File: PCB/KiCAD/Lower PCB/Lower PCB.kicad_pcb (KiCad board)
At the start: 2 copper layers, 188.6 x 165.4 mm, 106 parts, among them IC1 ADG608BRZ, IC2 ADG608BRZ, IC3 ADG608BRZ, J1 Conn_01x02_MountingPin, J2 Conn_01x04_MountingPin, J3 Conn_01x04_MountingPin, J4 Conn_01x04_MountingPin, Q1 SFH320, Q10 SFH320, Q11 SFH320, Q12 SFH320, Q13 SFH320, Q14 SFH320, Q15 SFH320, Q16 SFH320, Q17 SFH320, Q18 SFH320, Q19 SFH320, Q2 SFH320, Q20 SFH320, Q21 SFH320, Q22 SFH320, Q23 SFH320, Q24 SFH320, Q3 SFH320, Q4 SFH320, Q5 SFH320, Q6 SFH320, Q7 SFH320, Q8 SFH320, Q9 SFH320

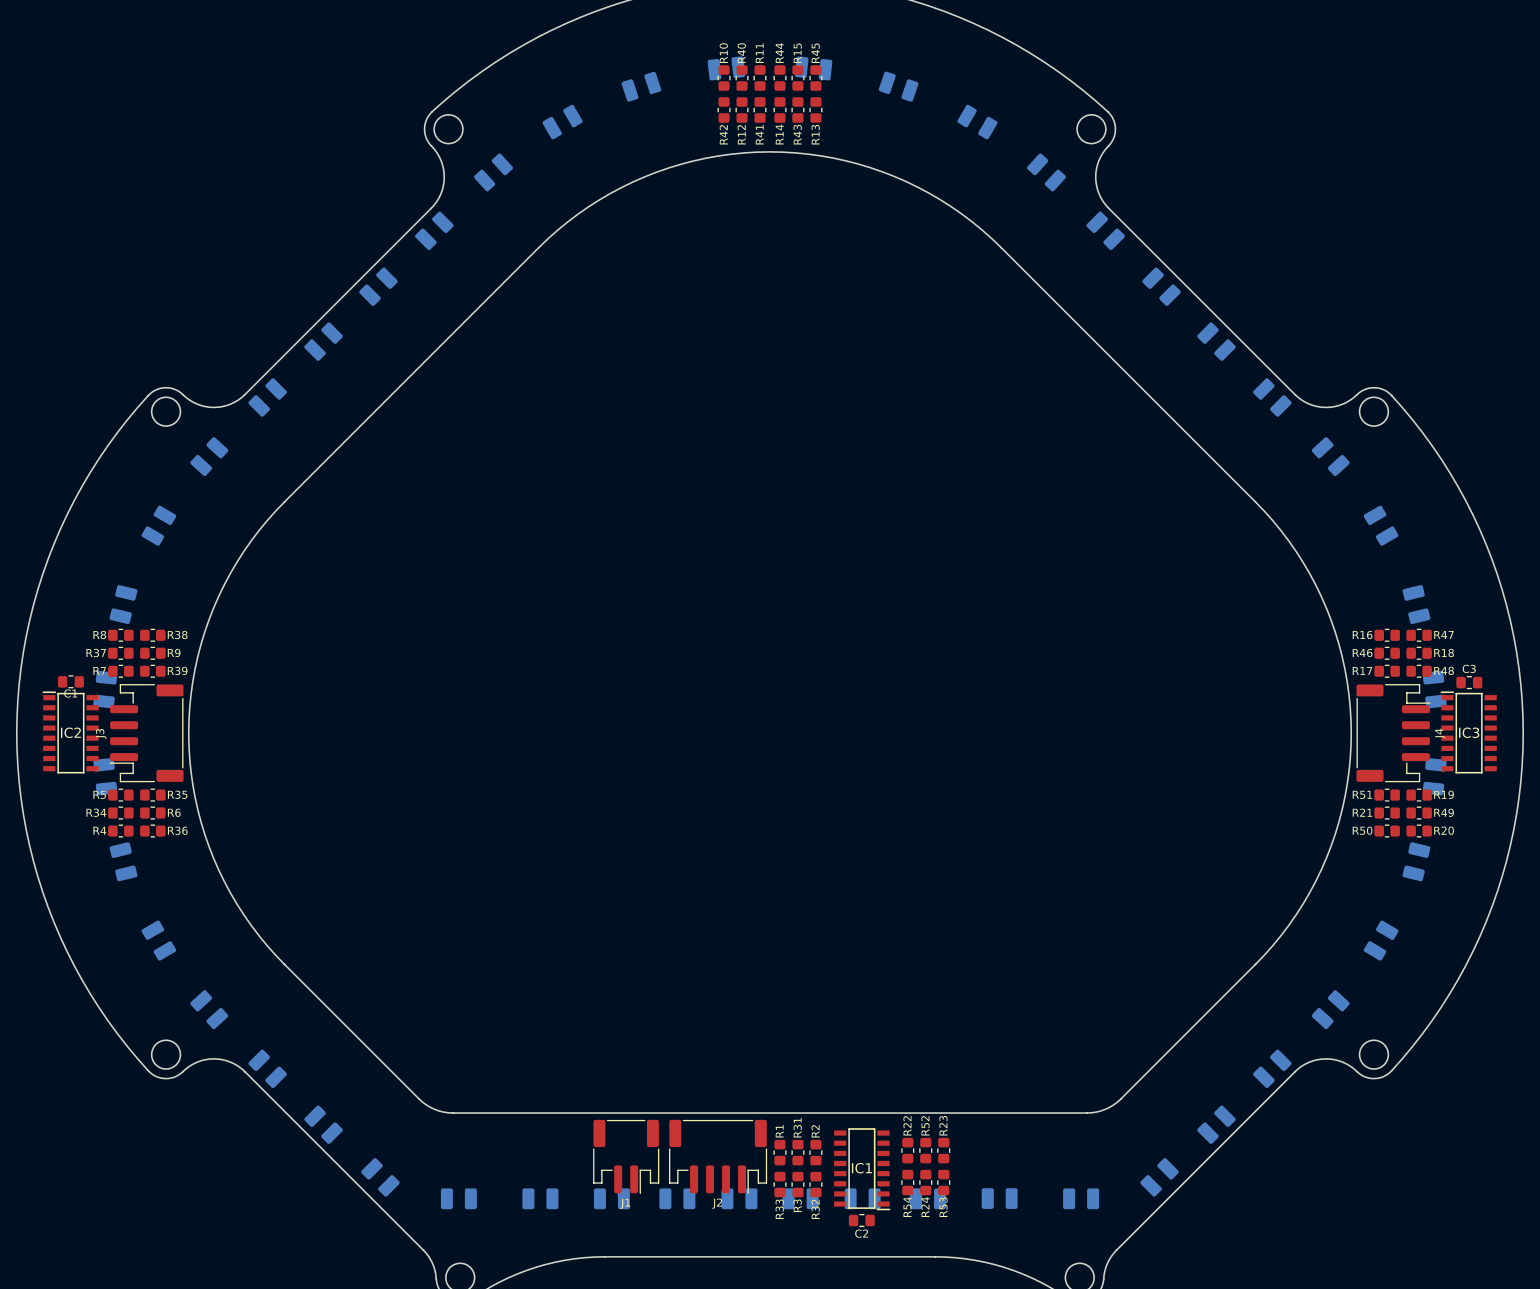
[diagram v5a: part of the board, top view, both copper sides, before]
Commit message: Started routing lower PCB
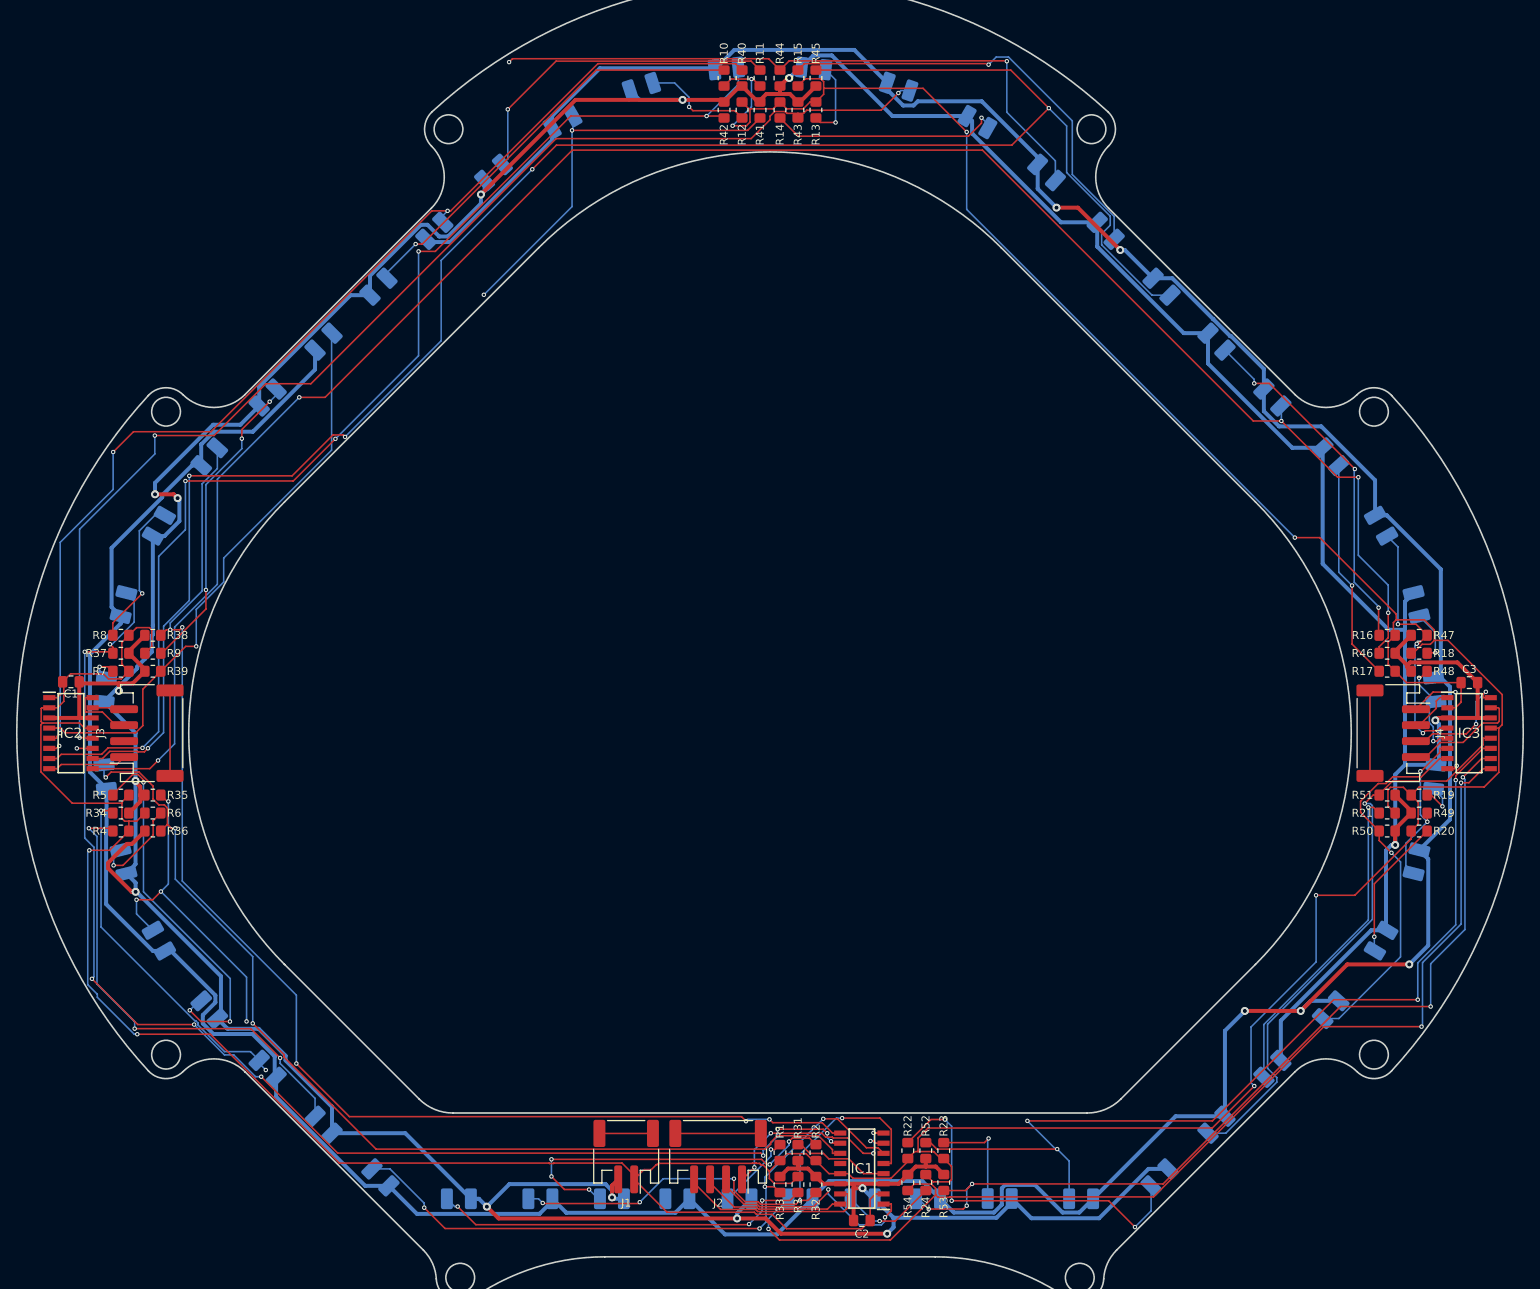
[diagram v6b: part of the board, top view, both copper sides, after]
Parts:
- turned D8 to 60 degrees
- turned Q5 to 120 degrees
- turned D20 to -121 degrees
- turned Q17 to -60 degrees
- turned D14 to -30 degrees
- turned Q11 to 30 degrees
- turned D11 to 42 degrees
- turned Q14 to -42 degrees
- turned D17 to -48 degrees
- turned Q20 to -132 degrees
- turned D5 to 132 degrees
- turned Q8 to 48 degrees
- turned D7 to 84 degrees
- turned Q6 to 96 degrees
- turned D19 to -96 degrees
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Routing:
- net GND: track 0.00 -> 681.4 mm, vias 0 -> 15
- net +3V3: track 0.00 -> 561.8 mm, vias 0 -> 8
- net +5V: track 0.00 -> 538.7 mm, vias 0 -> 5
- net Net-(IC2-S8): track 0.00 -> 249.7 mm, vias 0 -> 5
- net Net-(IC2-S7): track 0.00 -> 239.5 mm, vias 0 -> 5
- net Net-(IC1-S7): track 0.00 -> 160.8 mm, vias 0 -> 9
- net Net-(IC1-S8): track 0.00 -> 160.7 mm, vias 0 -> 5
- net Net-(IC2-S5): track 0.00 -> 156.8 mm, vias 0 -> 3
- net Net-(IC2-S4): track 0.00 -> 149.7 mm, vias 0 -> 5
- net Net-(IC2-S2): track 0.00 -> 140.6 mm, vias 0 -> 3
- net Net-(IC3-S8): track 0.00 -> 140.3 mm, vias 0 -> 3
- net Net-(IC1-S6): track 0.00 -> 127.6 mm, vias 0 -> 3
- net Net-(IC3-S6): track 0.00 -> 119.8 mm, vias 0 -> 4
- net Net-(IC3-S7): track 0.00 -> 115.6 mm, vias 0 -> 5
- net Net-(IC2-S6): track 0.00 -> 83.0 mm, vias 0 -> 3
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
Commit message: Traced lower PCB (mostly)
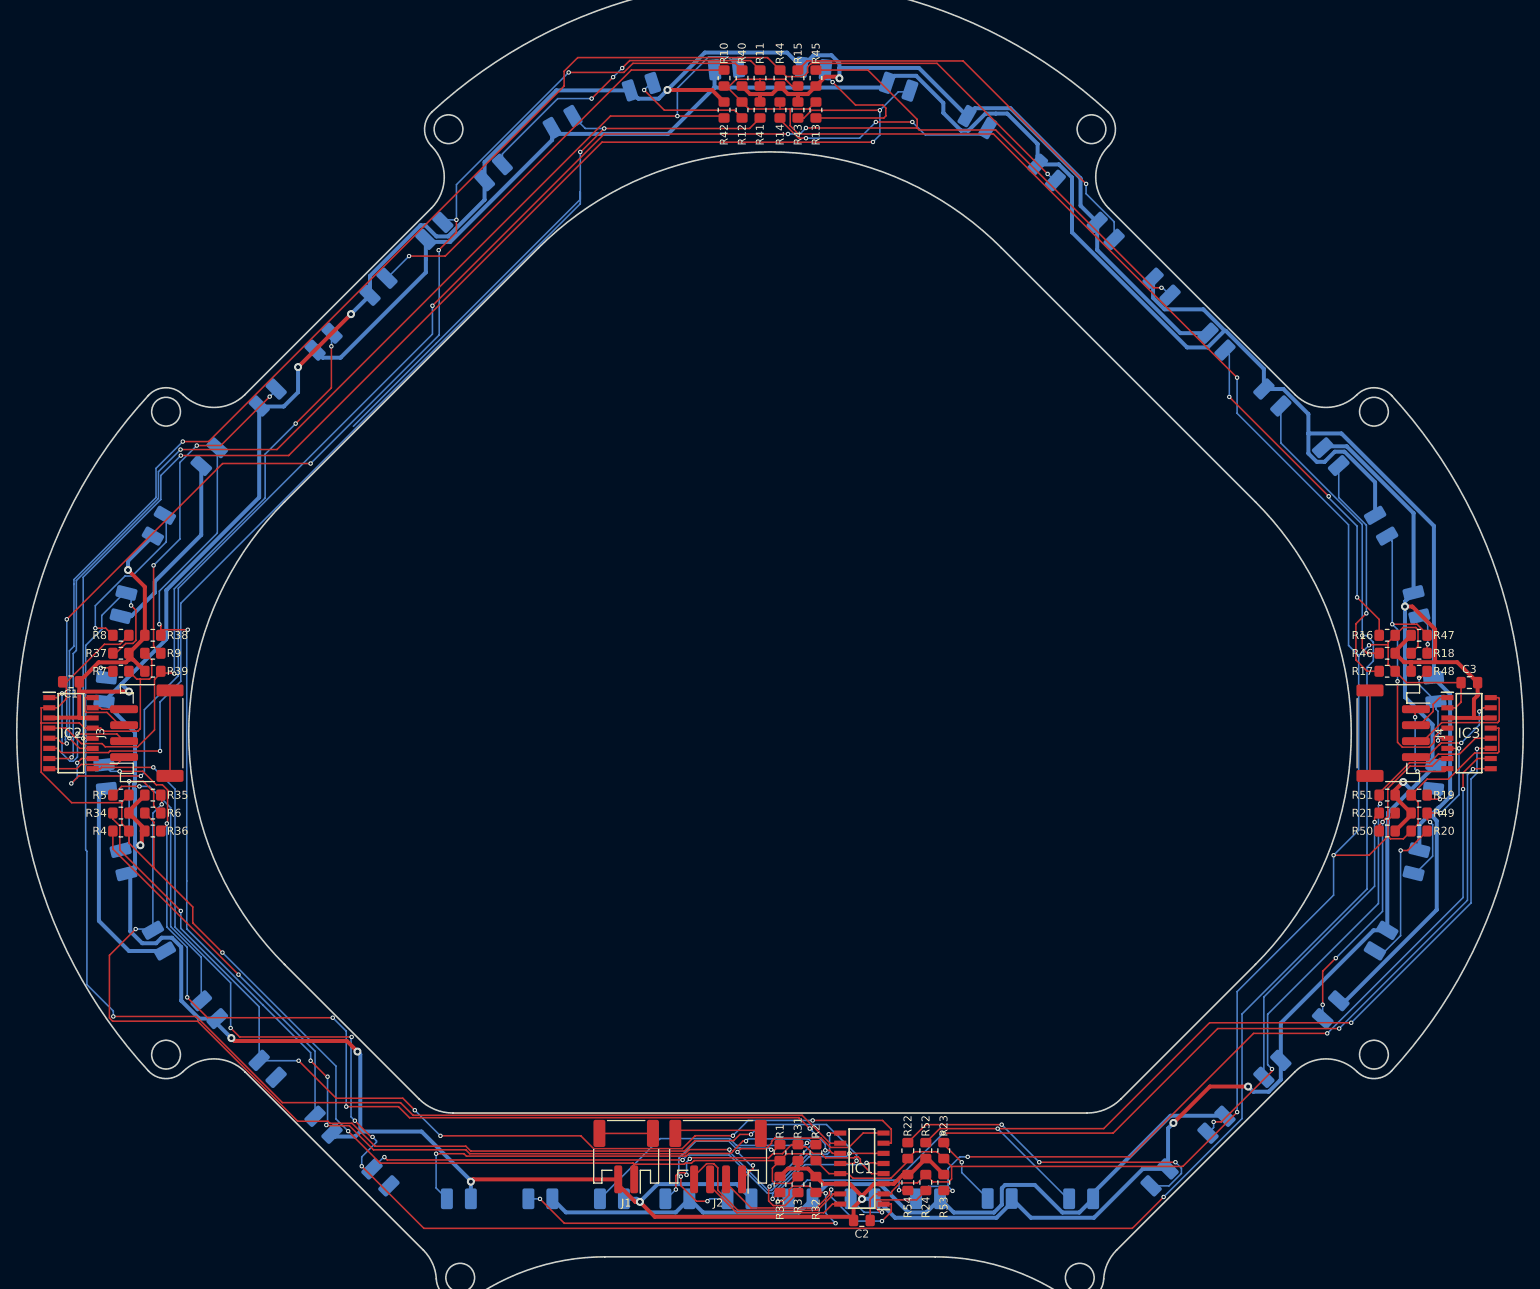
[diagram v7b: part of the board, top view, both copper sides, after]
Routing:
- net Net-(IC2-S3): track 52.6 -> 180.9 mm
- net Net-(IC2-S6): track 83.0 -> 184.8 mm
- net Net-(IC1-S5): track 41.8 -> 138.4 mm
- net +5V: track 538.7 -> 452.1 mm, vias 5 -> 0
- net Net-(IC1-S4): track 46.3 -> 126.9 mm, vias 3 -> 6
- net Net-(IC2-S8): track 249.7 -> 302.5 mm, vias 5 -> 8
- net +3V3: track 561.8 -> 534.8 mm, vias 8 -> 6
- net Net-(IC2-S7): track 239.5 -> 214.6 mm, vias 5 -> 7
- net Net-(IC1-S1): track 12.2 -> 34.1 mm, vias 0 -> 3
- net Net-(D3-A): track 47.7 -> 68.5 mm
- net LED_2_A0: track 1.59 -> 21.0 mm, vias 0 -> 2
- net GND: track 681.4 -> 700.9 mm, vias 15 -> 16
- net Net-(IC3-S8): track 140.3 -> 122.0 mm, vias 3 -> 4
- net Net-(D1-A): track 9.88 -> 24.6 mm, vias 1 -> 3
- net Net-(D2-A): track 44.7 -> 30.7 mm, vias 5 -> 1
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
